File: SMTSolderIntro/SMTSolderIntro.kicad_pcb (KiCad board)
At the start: 2 copper layers, 88.9 x 63.5 mm, 152 parts, among them J1 USB_C_PWR_THRU, J2 Barrel_Jack, U1 NE556, U2 M74LCX04, U3 NE556

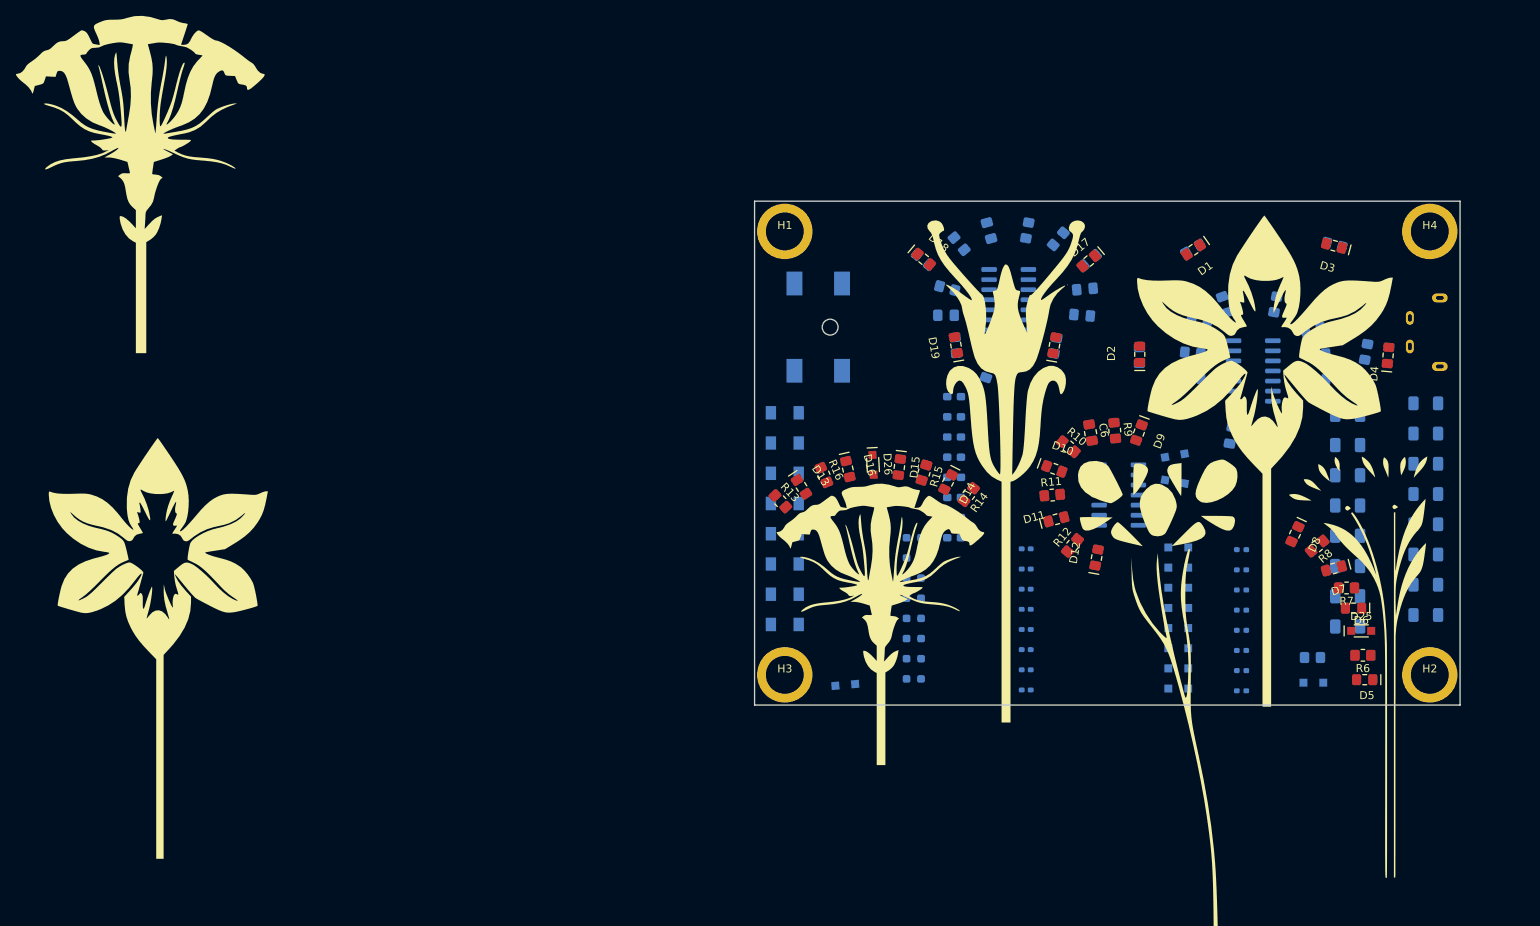
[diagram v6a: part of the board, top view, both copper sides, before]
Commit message: Component layout and routing traces
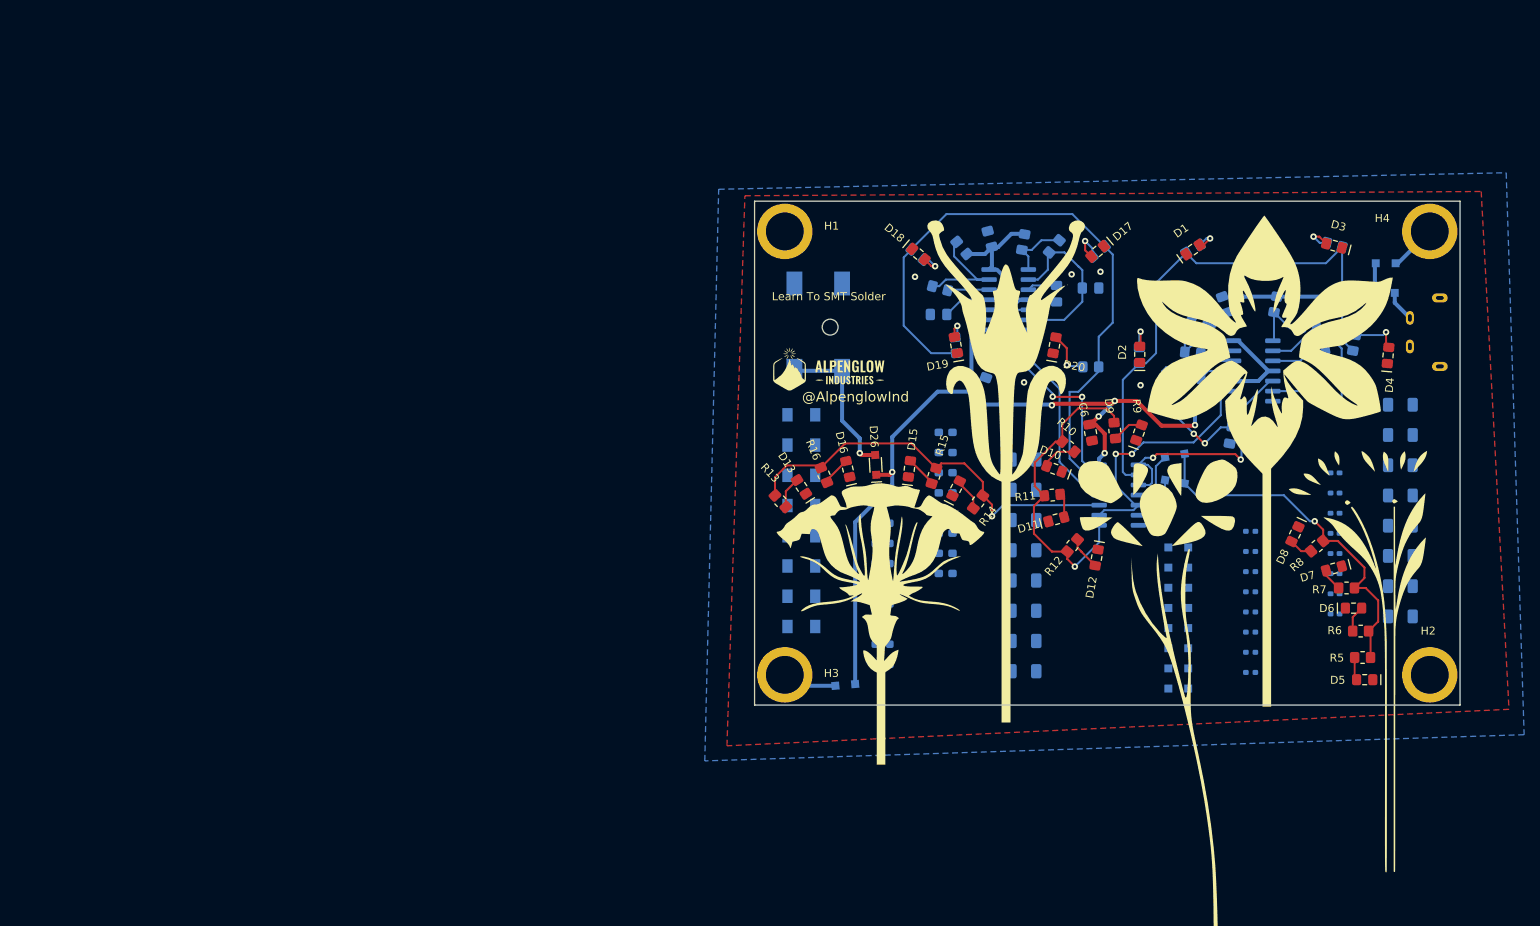
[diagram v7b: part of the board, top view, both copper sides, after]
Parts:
- removed the G*** at (38.2, 102.0)
- removed the G*** at (38.2, 101.1)
- removed the G*** at (36.5, 43.3)
- removed the G*** at (36.5, 43.2)
- added G***: LOGO, Alpenglow:Alpenglow_Logo_Horiz_15x6.2, F.Cu at (123.6, 67.0)
- D25: moved to B.Cu
- R5: moved to F.Cu
- moved D24 53.6 mm to (193.8, 53.5), turned to 0 degrees
- moved D25 42.7 mm to (193.7, 57.3)
- moved C12 41.2 mm to (148.2, 78.3)
- moved C13 41.2 mm to (148.2, 82.1)
- moved C14 41.2 mm to (148.2, 85.9)
- moved C15 41.2 mm to (148.2, 89.7)
- moved C16 41.2 mm to (148.2, 93.5)
- moved C17 41.2 mm to (148.2, 97.3)
- moved C18 41.2 mm to (148.2, 101.1)
- moved C19 41.2 mm to (148.2, 105.0)
- moved C28 40.1 mm to (187.5, 80.0)
- moved C29 40.1 mm to (187.5, 82.5)
- moved C30 40.1 mm to (187.5, 85.0)
- moved C31 40.1 mm to (187.5, 87.6)
- moved C32 40.1 mm to (187.5, 90.1)
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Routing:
- net +5V: track 0.00 -> 173.8 mm, vias 0 -> 8
- net /BLINK4: track 0.00 -> 81.1 mm
- net /BLINK1: track 0.00 -> 68.2 mm
- net /BLINK3: track 0.00 -> 51.9 mm, vias 0 -> 1
- net /BLINK5: track 0.00 -> 46.1 mm, vias 0 -> 1
- net /BLINK2: track 0.00 -> 39.3 mm, vias 0 -> 1
- net /CLK2: track 0.00 -> 32.7 mm, vias 0 -> 2
- net /CLK1: track 0.00 -> 31.0 mm, vias 0 -> 2
- net /CLK3: track 0.00 -> 29.9 mm
- net Net-(C4-Pad1): track 0.00 -> 29.4 mm, vias 0 -> 2
- net /CLK4: track 0.00 -> 28.8 mm, vias 0 -> 2
- net Net-(C2-Pad1): track 0.00 -> 28.3 mm
- net Net-(C8-Pad1): track 0.00 -> 22.1 mm
- net +Vbarrel: track 0.00 -> 19.3 mm, vias 0 -> 1
- net Net-(C10-Pad1): track 0.00 -> 17.5 mm, vias 0 -> 2
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- added copper zone on B.Cu, net GND
- added copper zone on F.Cu, net GND
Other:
- board text added: "@AlpenglowInd"
- board text added: "Learn To SMT Solder"

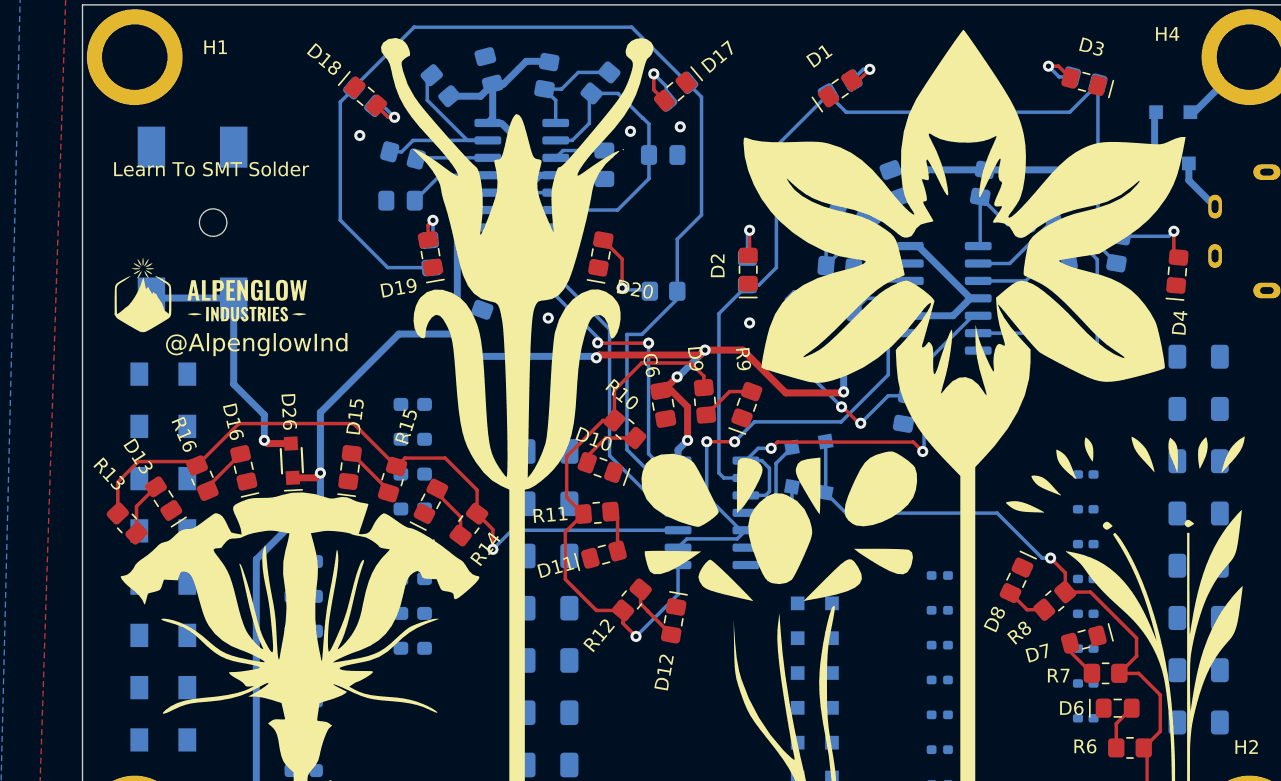
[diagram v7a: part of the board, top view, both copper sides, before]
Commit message: Adjusted refrence designators
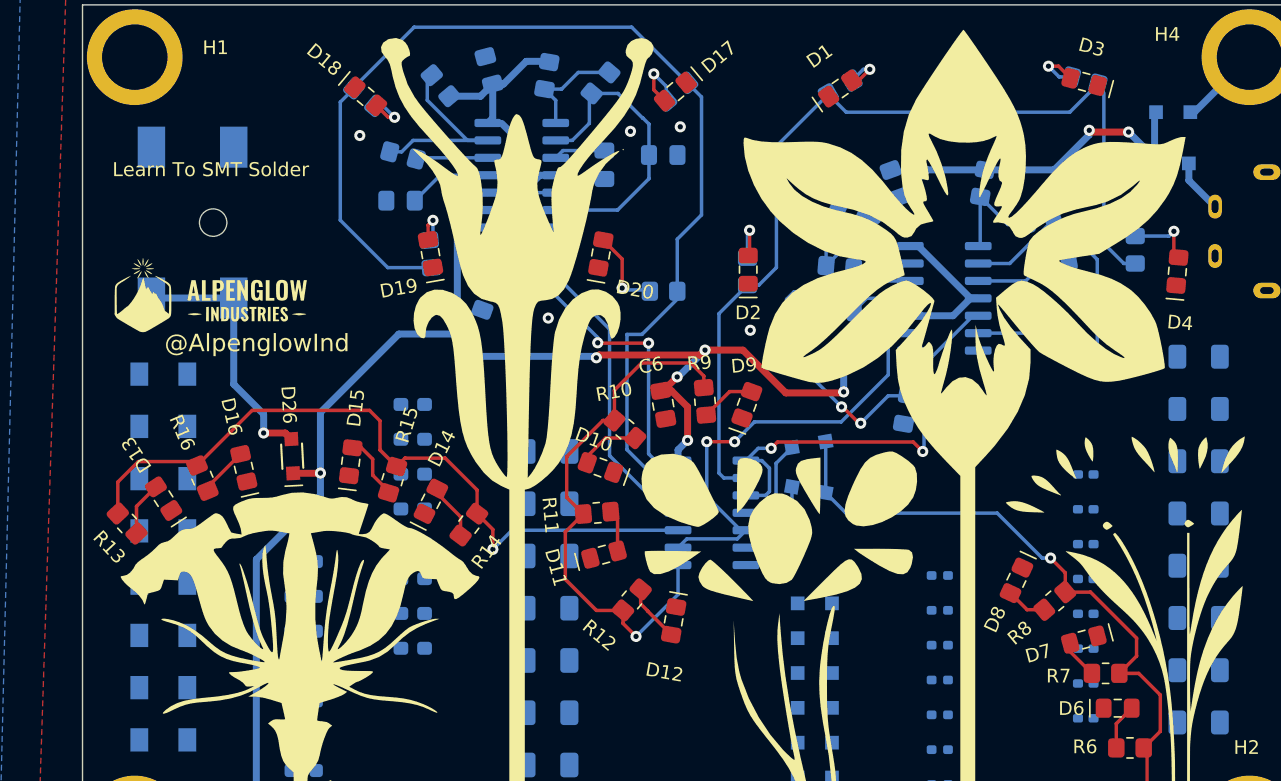
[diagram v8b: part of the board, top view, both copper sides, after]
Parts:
- moved R4 1.19 mm to (191.1, 63.6), turned to 90 degrees
- moved D15 0.42 mm to (133.9, 79.0)
- moved D26 0.33 mm to (129.6, 78.6)
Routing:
- net +5V: track 173.8 -> 176.0 mm
- net /BLINK3: track 51.9 -> 53.9 mm
- net Net-(D4-PadA): track 6.04 -> 5.02 mm
- net Net-(D15-PadA): track 3.97 -> 4.93 mm
